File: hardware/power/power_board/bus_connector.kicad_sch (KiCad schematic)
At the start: 2 parts, among them J701 504050-1291, J702 504050-0491

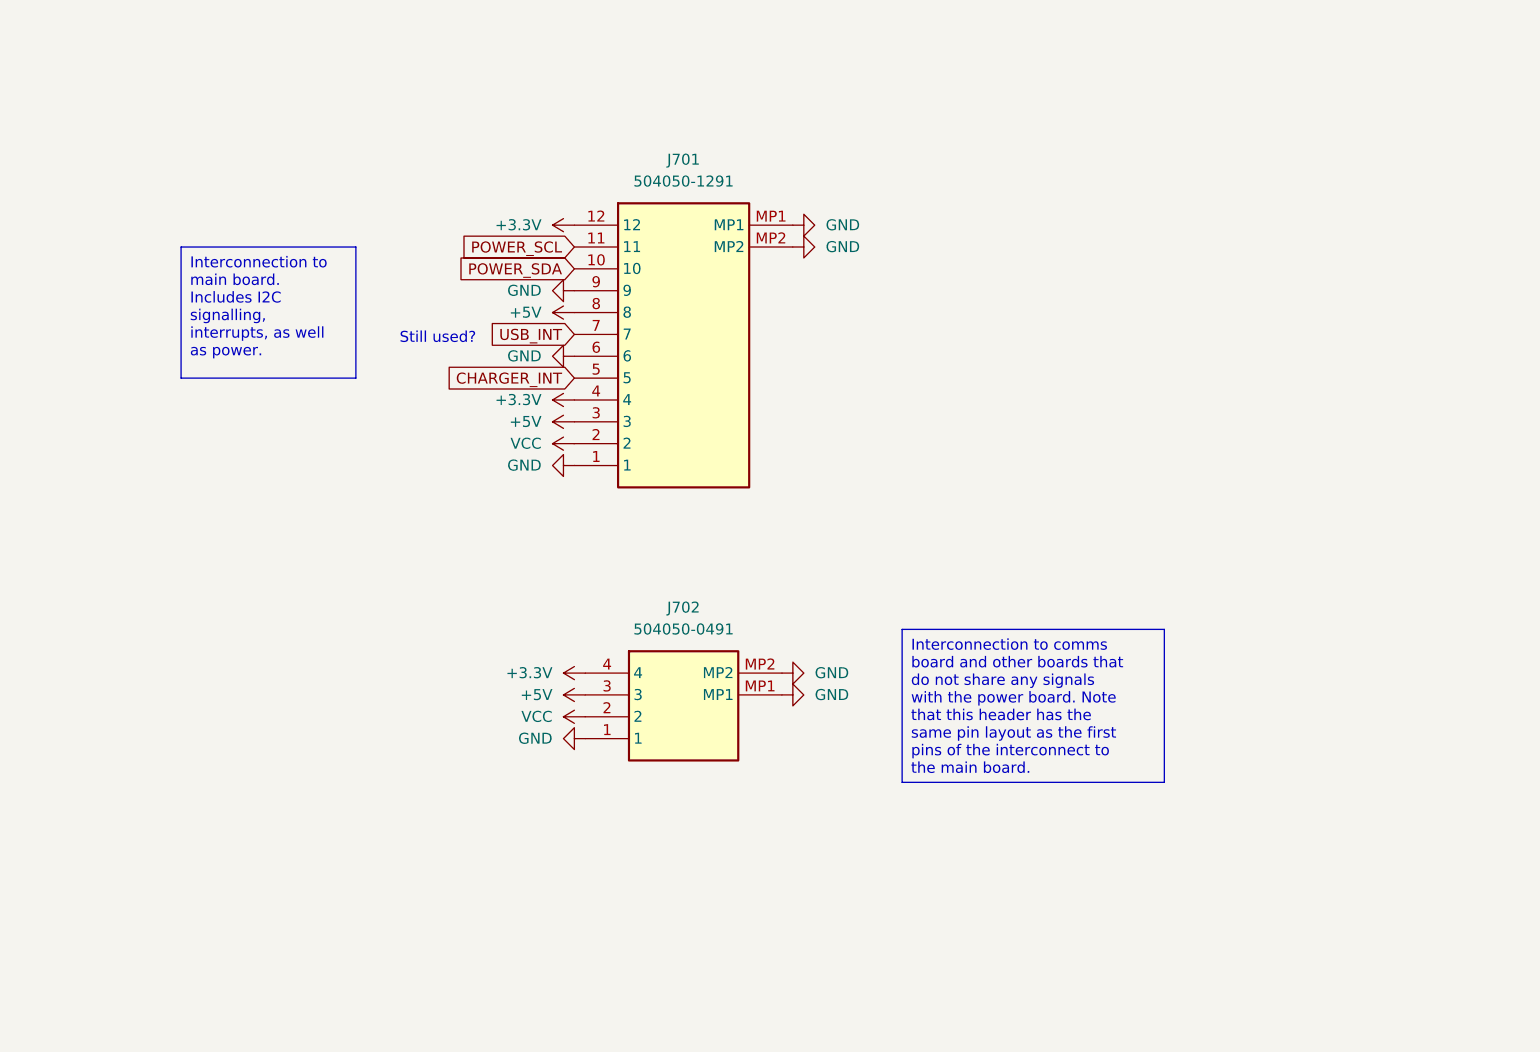
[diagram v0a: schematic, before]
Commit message: Changed interconnect from battery to power board to use the 10-pin Pico-Lock receptacle and cable.
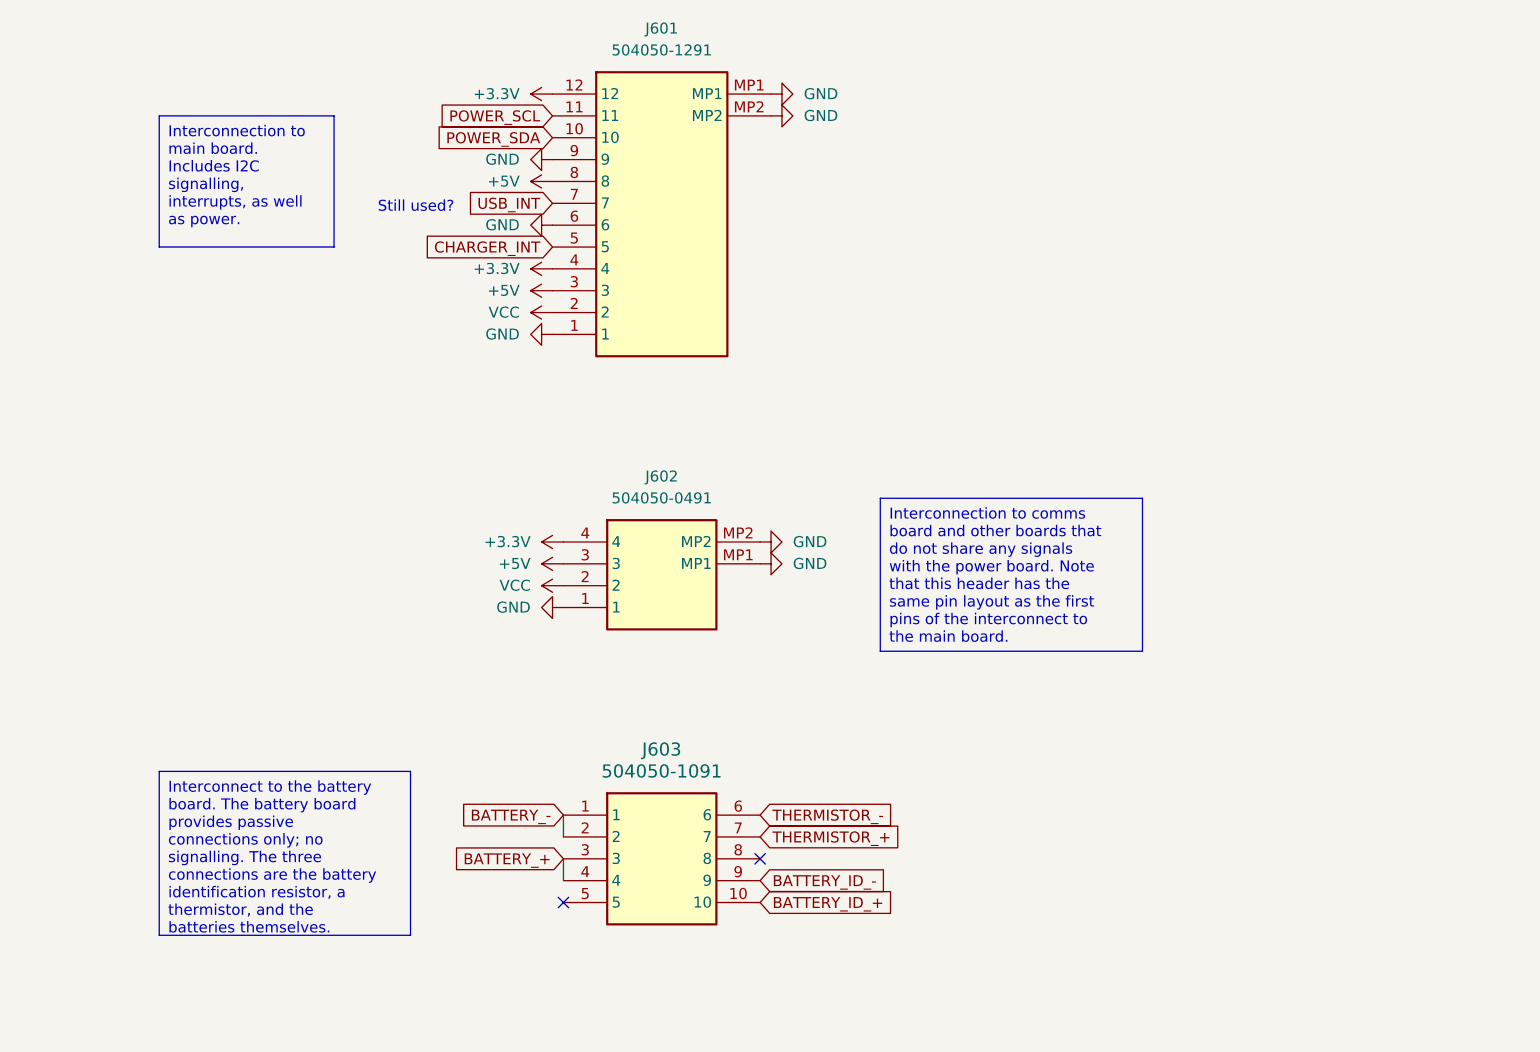
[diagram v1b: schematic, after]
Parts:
- added J603: 504050-1091, footprints:504050-1091, symbol Molex 504050-1091:504050-1091
- renumbered J701 to J601, J702 to J602
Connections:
- new net BATTERY_+: J603.3, J603.4
- new net BATTERY_-: J603.1, J603.2
- new net BATTERY_ID_+: J603.10
- new net BATTERY_ID_-: J603.9
- new net THERMISTOR_+: J603.7
- new net THERMISTOR_-: J603.6
- no-connect marks 0 -> 2
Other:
- moved on the sheet: J601, J602

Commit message: Checkpointing work on laying out the power board
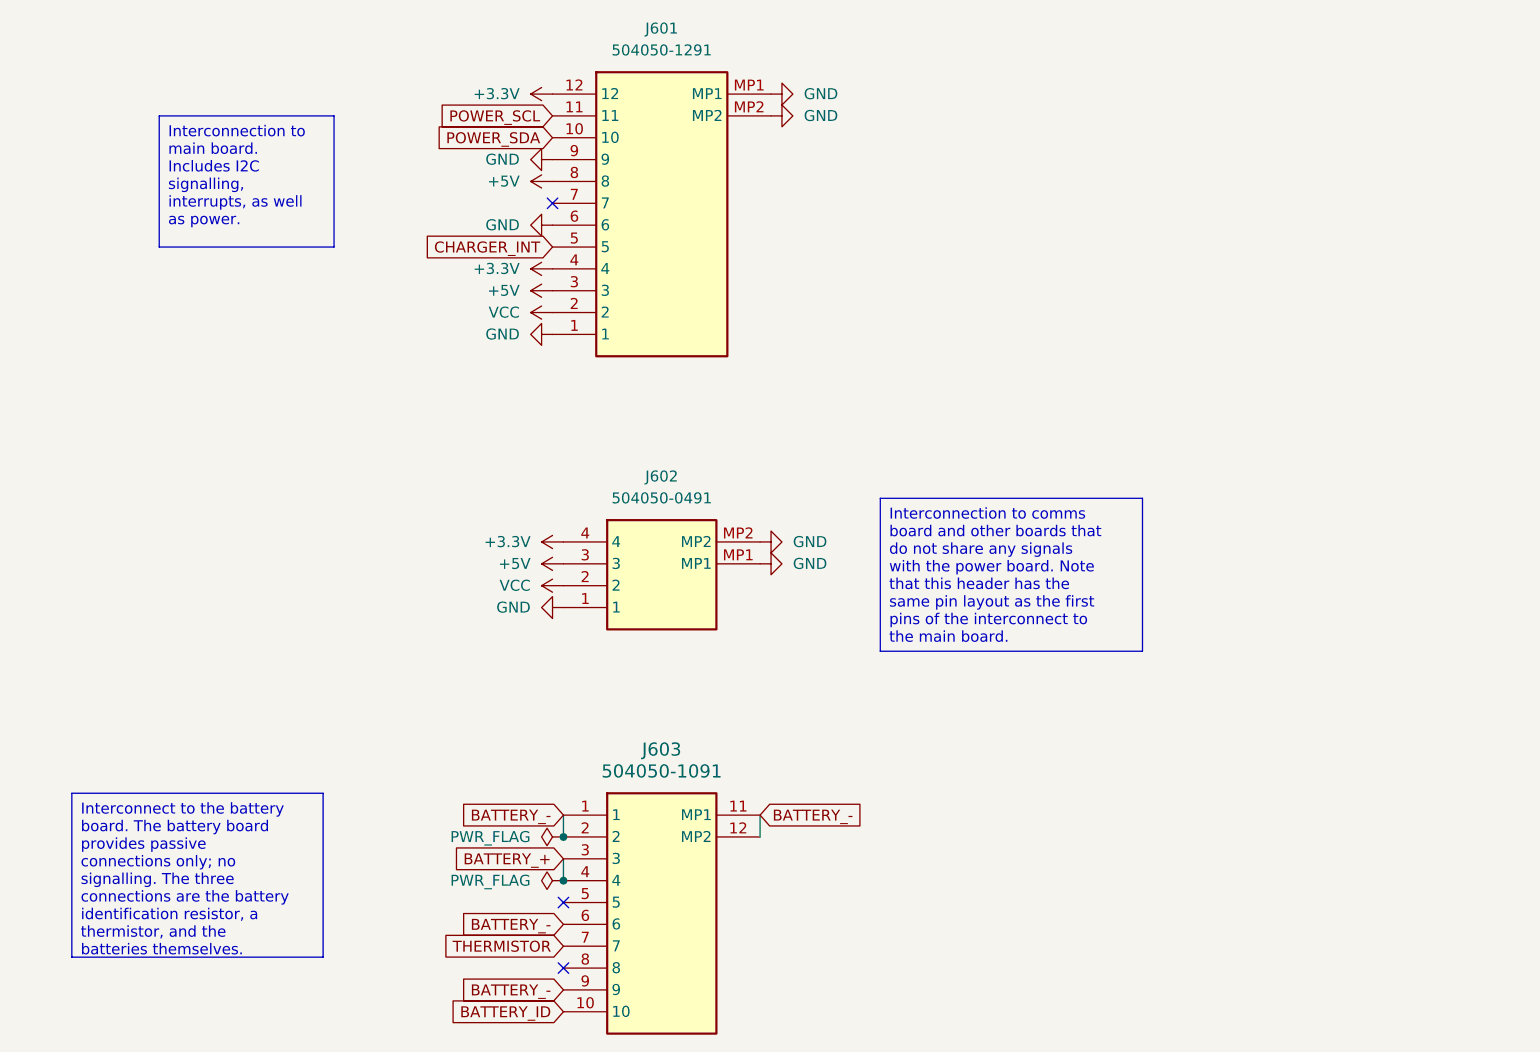
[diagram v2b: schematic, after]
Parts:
- J601: footprint footprints:5040501291 -> 5040501291
- J602: footprint footprints:5040500491 -> 5040500491
- J603: footprint footprints:504050-1091 -> 504050-1091; Active (none) -> Y
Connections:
- net BATTERY_ID_- is gone; now on net BATTERY_-: J603.9
- net THERMISTOR_- is gone; now on net BATTERY_-: J603.6
- net BATTERY_-: now also J603.11 (MP1), J603.12 (MP2)
- net BATTERY_ID_+ renamed BATTERY_ID
- net THERMISTOR_+ renamed THERMISTOR
- net USB_INT: no longer names the net of J601.7
- no-connect marks 2 -> 3
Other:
- note removed: "Still used?"
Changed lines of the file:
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@@
 (kicad_sch (version 20230121) (generator eeschema)
   (paper "USLetter")
-  (no_connect (at 151.13 134.62))
+  (junction (at 128.27 132.08) (diameter 0) (color 0 0 0 0)
+  )
+  (junction (at 128.27 137.16) (diameter 0) (color 0 0 0 0)
+  )
+  (no_connect (at 127 58.42))
+  (no_connect (at 128.27 147.32))
   (no_connect (at 128.27 139.7))
+  (wire (pts (xy 151.13 129.54) (xy 151.13 132.08))
+    (stroke (width 0) (type default))
+  )
   (wire (pts (xy 128.27 129.54) (xy 128.27 132.08))
     (stroke (width 0) (type default))
@@
   )
   (text_box "Interconnect to the battery board. The battery board provides passive connections only; no signalling. The three connections are the battery identification resistor, a thermistor, and the batteries themselves."
-    (at 81.28 124.46 0) (size 29.21 19.05)
+    (at 71.12 127 0) (size 29.21 19.05)
     (stroke (width 0) (type default))
     (fill (type none))
@@
     (effects (font (size 1.27 1.27)) (justify left top))
   )
-  (text "Still used?\n" (at 106.68 59.69 0)
-    (effects (font (size 1.27 1.27)) (justify left bottom))
+  (global_label "BATTERY_-" (shape input) (at 151.13 129.54 0) (fields_autoplaced)
+    (effects (font (size 1.27 1.27)) (justify left))
+    (property "Intersheetrefs" "${INTERSHEET_REFS}" (at 164.4566 129.54 0)
+      (effects (font (size 1.27 1.27)) (justify left))
+    )
   )
   (global_label "BATTERY_-" (shape input) (at 128.27 129.54 180) (fields_autoplaced)
     (effects (font (size 1.27 1.27)) (justify right))
     (property "Intersheetrefs" "${INTERSHEET_REFS}" (at 114.9434 129.54 0)
-      (effects (font (size 1.27 1.27)) (justify right) hide)
-    )
-  )
-  (global_label "BATTERY_ID_-" (shape input) (at 151.13 137.16 0) (fields_autoplaced)
-    (effects (font (size 1.27 1.27)) (justify left))
-    (property "Intersheetrefs" "${INTERSHEET_REFS}" (at 167.299 137.16 0)
-      (effects (font (size 1.27 1.27)) (justify left) hide)
-    )
-  )
-  (global_label "THERMISTOR_-" (shape input) (at 151.13 129.54 0) (fields_autoplaced)
-    (effects (font (size 1.27 1.27)) (justify left))
-    (property "Intersheetrefs" "${INTERSHEET_REFS}" (at 168.2061 129.54 0)
-      (effects (font (size 1.27 1.27)) (justify left) hide)
-    )
-  )
-  (global_label "USB_INT" (shape input) (at 127 58.42 180) (fields_autoplaced)
-    (effects (font (size 1.27 1.27)) (justify right))
-    (property "Intersheetrefs" "${INTERSHEET_REFS}" (at 116.3343 58.42 0)
-      (effects (font (size 1.27 1.27)) (justify right) hide)
+      (effects (font (size 1.27 1.27)) (justify right))
+    )
+  )
+  (global_label "THERMISTOR" (shape input) (at 128.27 144.78 180) (fields_autoplaced)
+    (effects (font (size 1.27 1.27)) (justify right))
+    (property "Intersheetrefs" "${INTERSHEET_REFS}" (at 113.7339 144.78 0)
+      (effects (font (size 1.27 1.27)) (justify right))
+    )
+  )
+  (global_label "BATTERY_-" (shape input) (at 128.27 149.86 180) (fields_autoplaced)
+    (effects (font (size 1.27 1.27)) (justify right))
+    (property "Intersheetrefs" "${INTERSHEET_REFS}" (at 114.9434 149.86 0)
+      (effects (font (size 1.27 1.27)) (justify right))
     )
   )
@@
     (effects (font (size 1.27 1.27)) (justify right))
     (property "Intersheetrefs" "${INTERSHEET_REFS}" (at 113.0082 50.8 0)
-      (effects (font (size 1.27 1.27)) (justify right) hide)
-    )
-  )
-  (global_label "BATTERY_ID_+" (shape input) (at 151.13 139.7 0) (fields_autoplaced)
-    (effects (font (size 1.27 1.27)) (justify left))
-    (property "Intersheetrefs" "${INTERSHEET_REFS}" (at 167.299 139.7 0)
-      (effects (font (size 1.27 1.27)) (justify left) hide)
-    )
-  )
-  (global_label "THERMISTOR_+" (shape input) (at 151.13 132.08 0) (fields_autoplaced)
-    (effects (font (size 1.27 1.27)) (justify left))
-    (property "Intersheetrefs" "${INTERSHEET_REFS}" (at 168.2061 132.08 0)
-      (effects (font (size 1.27 1.27)) (justify left) hide)
+      (effects (font (size 1.27 1.27)) (justify right))
+    )
+  )
+  (global_label "BATTERY_ID" (shape input) (at 128.27 152.4 180) (fields_autoplaced)
+    (effects (font (size 1.27 1.27)) (justify right))
+    (property "Intersheetrefs" "${INTERSHEET_REFS}" (at 114.641 152.4 0)
+      (effects (font (size 1.27 1.27)) (justify right))
+    )
+  )
+  (global_label "BATTERY_-" (shape input) (at 128.27 142.24 180) (fields_autoplaced)
+    (effects (font (size 1.27 1.27)) (justify right))
+    (property "Intersheetrefs" "${INTERSHEET_REFS}" (at 114.9434 142.24 0)
+      (effects (font (size 1.27 1.27)) (justify right))
     )
   )
@@
     (effects (font (size 1.27 1.27)) (justify right))
     (property "Intersheetrefs" "${INTERSHEET_REFS}" (at 113.0687 48.26 0)
-      (effects (font (size 1.27 1.27)) (justify right) hide)
+      (effects (font (size 1.27 1.27)) (justify right))
     )
   )
@@
     (effects (font (size 1.27 1.27)) (justify right))
     (property "Intersheetrefs" "${INTERSHEET_REFS}" (at 114.9434 134.62 0)
-      (effects (font (size 1.27 1.27)) (justify right) hide)
+      (effects (font (size 1.27 1.27)) (justify right))
     )
   )
@@
     (effects (font (size 1.27 1.27)) (justify right))
     (property "Intersheetrefs" "${INTERSHEET_REFS}" (at 111.4962 63.5 0)
-      (effects (font (size 1.27 1.27)) (justify right) hide)
+      (effects (font (size 1.27 1.27)) (justify right))
     )
   )
@@
       (effects (font (size 1.27 1.27)))
     )
-    (property "Footprint" "footprints:5040501291" (at 148.59 140.64 0)
+    (property "Footprint" "5040501291" (at 148.59 140.64 0)
       (effects (font (size 1.27 1.27)) (justify left top) hide)
     )
@@
       (effects (font (size 1.27 1.27)))
     )
-    (property "Footprint" "footprints:5040500491" (at 147.32 192.71 0)
+    (property "Footprint" "5040500491" (at 147.32 192.71 0)
       (effects (font (size 1.27 1.27)) (justify left top) hide)
     )
@@
     )
   )
+  (symbol (lib_id "power:PWR_FLAG") (at 128.27 132.08 90) (unit 1)
+    (in_bom yes) (on_board yes) (dnp no) (fields_autoplaced)
+    (property "Reference" "#FLG0601" (at 126.365 132.08 0)
+      (effects (font (size 1.27 1.27)) hide)
+    )
+    (property "Value" "PWR_FLAG" (at 124.46 132.08 90)
+      (effects (font (size 1.27 1.27)) (justify left))
+    )
+    (property "Footprint" "" (at 128.27 132.08 0)
+      (effects (font (size 1.27 1.27)) hide)
+    )
+    (property "Datasheet" "~" (at 128.27 132.08 0)
+      (effects (font (size 1.27 1.27)) hide)
+    )
+    (pin "1")
+    (instances
+      (project "power_board"
+        (path "/d7fbba2e-84c5-4e09-9d36-52dae726d12d/f5dda946-81da-4978-88f4-4ac2bc2b63d0"
+          (reference "#FLG0601") (unit 1)
+        )
+      )
+    )
+  )
+  (symbol (lib_id "power:PWR_FLAG") (at 128.27 137.16 90) (unit 1)
+    (in_bom yes) (on_board yes) (dnp no) (fields_autoplaced)
+    (property "Reference" "#FLG0602" (at 126.365 137.16 0)
+      (effects (font (size 1.27 1.27)) hide)
+    )
+    (property "Value" "PWR_FLAG" (at 124.46 137.16 90)
+      (effects (font (size 1.27 1.27)) (justify left))
+    )
+    (property "Footprint" "" (at 128.27 137.16 0)
+      (effects (font (size 1.27 1.27)) hide)
+    )
+    (property "Datasheet" "~" (at 128.27 137.16 0)
+      (effects (font (size 1.27 1.27)) hide)
+    )
+    (pin "1")
+    (instances
+      (project "power_board"
+        (path "/d7fbba2e-84c5-4e09-9d36-52dae726d12d/f5dda946-81da-4978-88f4-4ac2bc2b63d0"
+          (reference "#FLG0602") (unit 1)
+        )
+      )
+    )
+  )
   (symbol (lib_id "Molex 504050-1091:504050-1091") (at 128.27 129.54 0) (unit 1)
     (in_bom yes) (on_board yes) (dnp no) (fields_autoplaced)
@@
       (effects (font (size 1.524 1.524)))
     )
-    (property "Footprint" "footprints:504050-1091" (at 147.32 224.46 0)
+    (property "Footprint" "504050-1091" (at 147.32 224.46 0)
       (effects (font (size 1.27 1.27)) (justify left top) hide)
     )
@@
     (property "Arrow Price/Stock" "" (at 147.32 1124.46 0)
       (effects (font (size 1.27 1.27)) (justify left top) hide)
+    )
+    (property "Active" "Y" (at 128.27 129.54 0)
+      (effects (font (size 1.27 1.27)) hide)
     )
     (pin "8")
@@
     (pin "10")
     (pin "9")
-    (instances
-      (project "power_board"
+    (pin "11")
+    (pin "12")
+    (instances
+      (project "power_board"

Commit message: Checkpointing layout work
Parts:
- removed J602: 504050-0491, 5040500491, symbol Molex 504050-0491:504050-0491
- added M601, M602, M603, M604: ~, MountingHole:MountingHole_3.2mm_M3_ISO7380_Pad_TopBottom, symbol mounting:Mounting_Hole_M3_ISO_7380
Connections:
- net GND: now also M601.1 (Hole), M602.1 (Hole), M603.1 (Hole), M604.1 (Hole)
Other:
- moved on the sheet: J601, J603
